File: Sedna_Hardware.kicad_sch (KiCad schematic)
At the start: 51 parts, among them J1 PJ-102A, J10 5-103634-2, J11 2-644488-2, J2 61201021721, J3 PPTC141LFBN-RC, J4 0878340619, J5 2-644803-3, J6 2-644488-3, J7 1935161, J8 1935161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

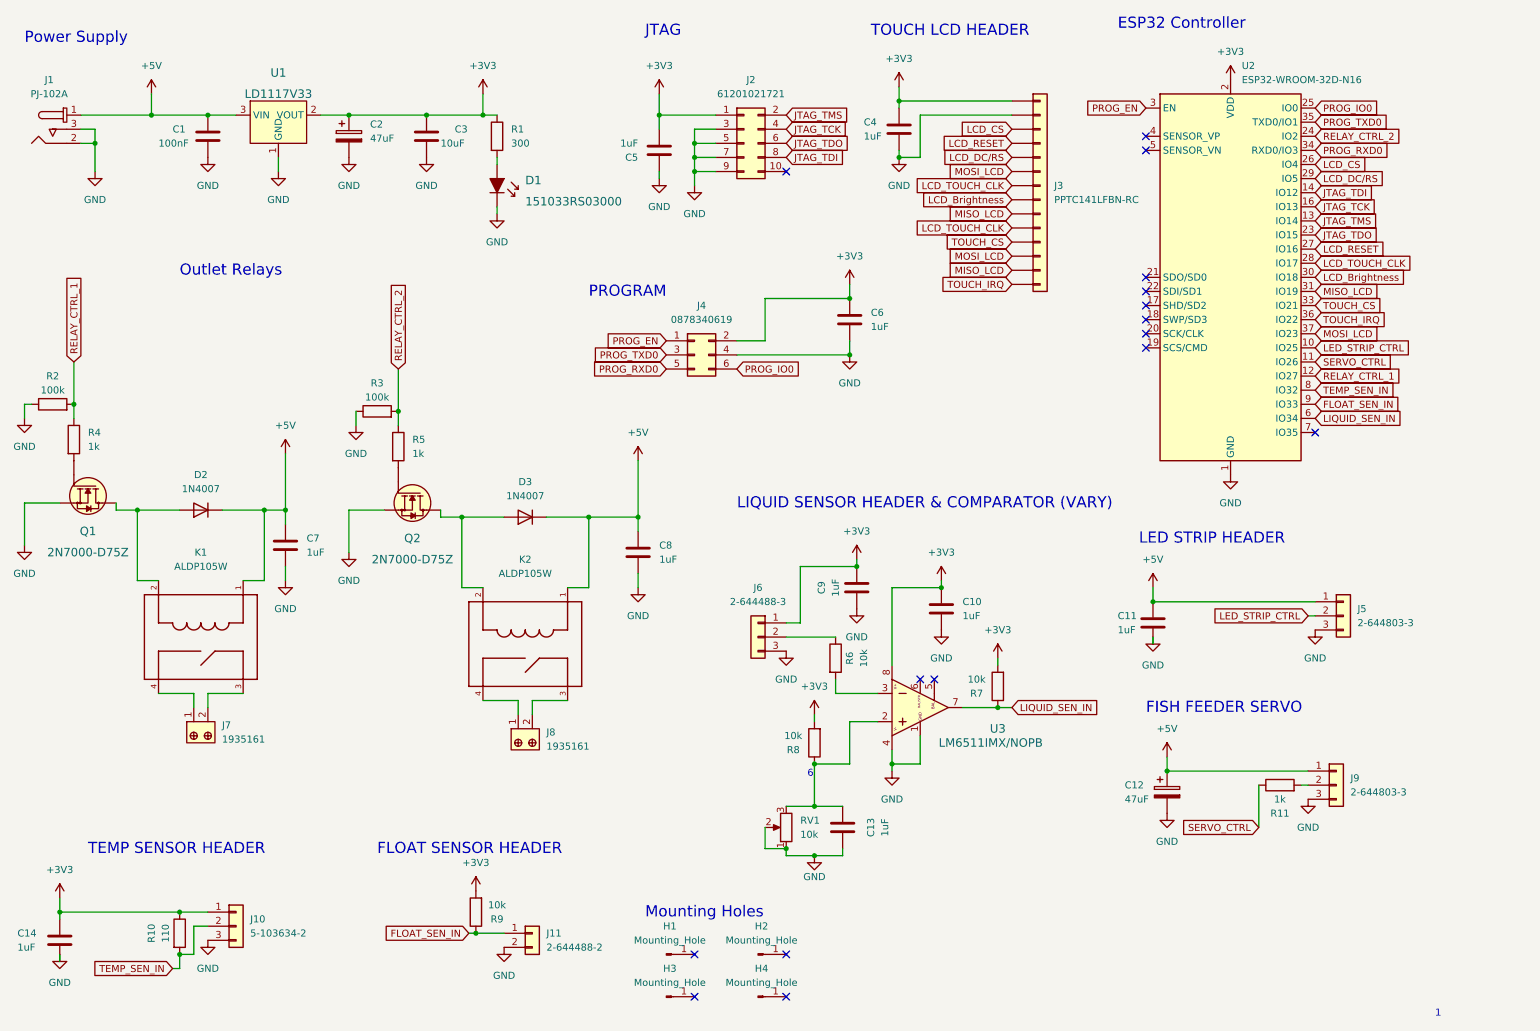
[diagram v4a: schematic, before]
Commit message: associated resistor and capacitor to DigiKey Procduct. Modified 1uf cap's footpring
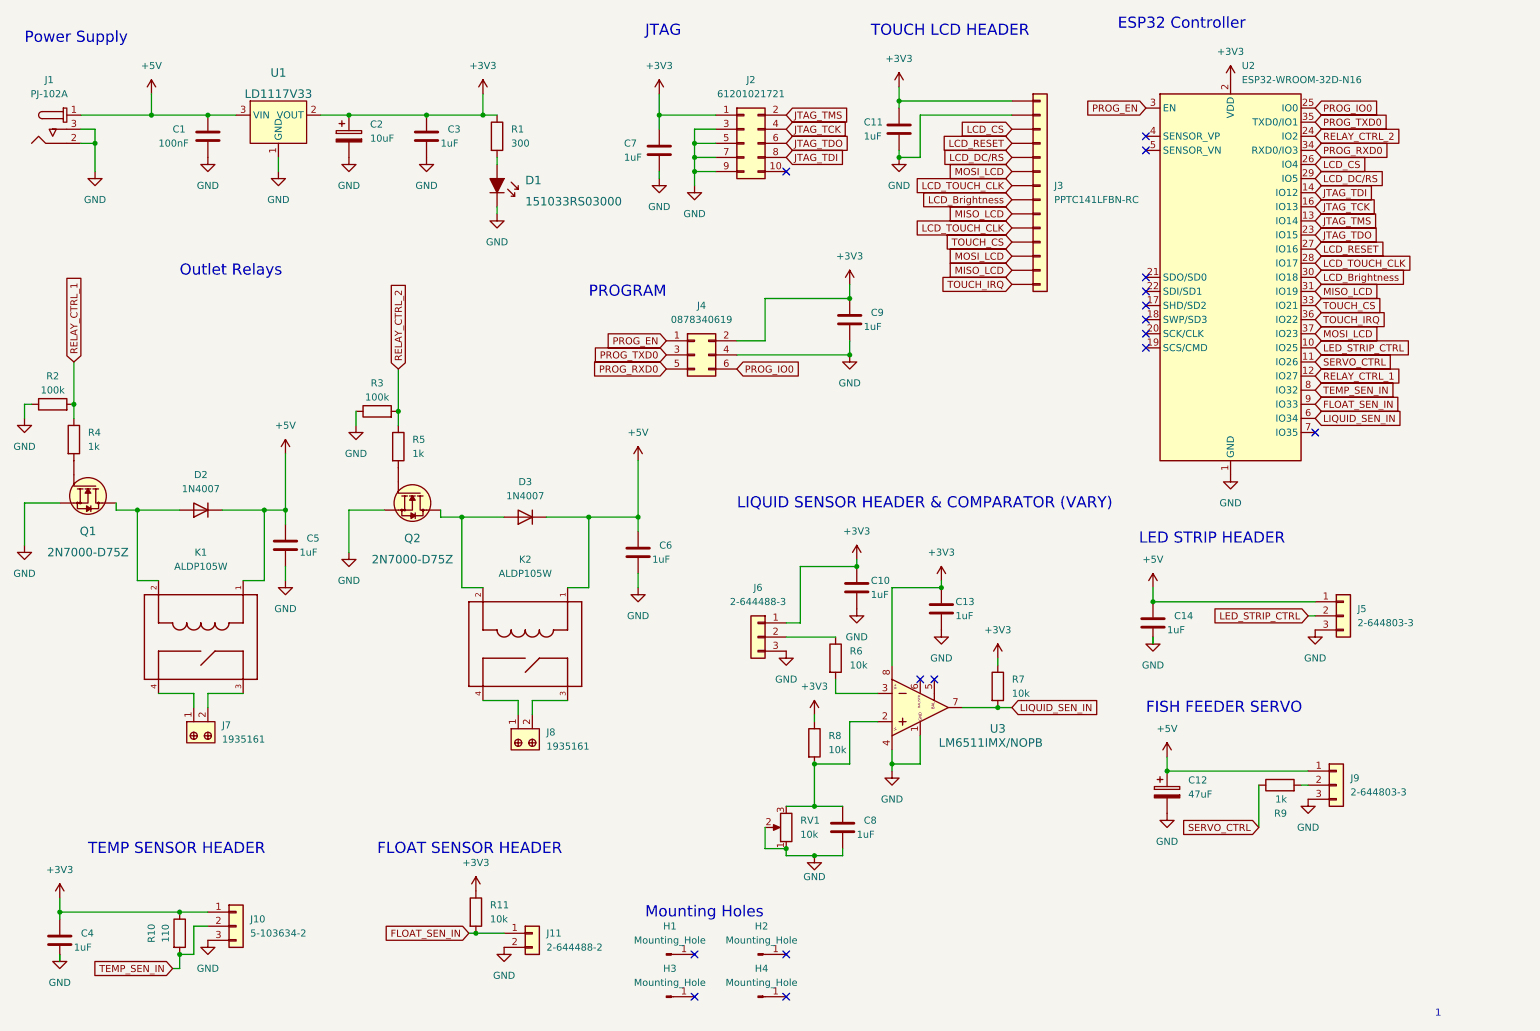
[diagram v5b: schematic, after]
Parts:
- C1: footprint Capacitor_THT:C_Disc_D9.0mm_W5.0mm_P5.00mm -> Capacitor_THT:C_Radial_D6.3mm_H5.0mm_P2.50mm; Category (none) -> Ceramic Capacitors; DK_Datasheet_LInk (none) -> https://www.vishay.com/docs/45171/kseries.pdf; DK_Detail_Page (none) -> https://www.digikey.ca/en/products/detail/vishay-beyschlag-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; Digi-key_PN (none) -> BC3324-ND; MPN (none) -> K104K15X7RF53L2; Manufacturer (none) -> Vishay Beyschlag/Draloric/BC Components; Status (none) -> active
- C10, C11, C13, C14, C4, C5, C6, C7, C8, C9: footprint Capacitor_THT:C_Disc_D9.0mm_W5.0mm_P5.00mm -> Capacitor_THT:C_Axial_L3.8mm_D2.6mm_P7.50mm_Horizontal; Category (none) -> Ceramic Capacitors; DK_Datasheet_Link (none) -> https://content.kemet.com/datasheets/KEM_C1041_AXIMAX_X7R.p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; DK_Detail_Page (none) -> https://www.digikey.ca/en/products/detail/kemet/C410C105K3R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; Digi-Key_PN (none) -> 399-C410C105K3R5TA-ND; MPN (none) -> C410C105K3R5TA; Manufacturer (none) -> KEMET; Status (none) -> active
- C12: Category (none) -> Aluminum Electrolytic Capacitors; DK_Datasheet_Link (none) -> https://media.digikey.com/pdf/Data%20Sheets/Panasonic%20Ele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; DK_Detail_Page (none) -> https://www.digikey.ca/en/products/detail/panasonic-electro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; Digi-Key_PN (none) -> P10417TB-ND; MPN (none) -> ECA-1VM470I; Manufacturer (none) -> Panasonic Electronic Components; Status (none) -> active
- C2: value 47uF -> 10uF; Category (none) -> Aluminum Electrolytic Capacitors; DK_Datasheet_Link (none) -> https://media.digikey.com/pdf/Data%20Sheets/Panasonic%20Ele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; DK_Detail_Page (none) -> https://www.digikey.ca/en/products/detail/kyocera-avx/TAP10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; Digi-Key_PN (none) -> 478-1839-ND; MPN (none) -> TAP106K016SCS; Manufacturer (none) -> KYOCERA AVX; Status (none) -> active
- C3: value 10uF -> 1uF; footprint Capacitor_THT:C_Disc_D9.0mm_W5.0mm_P5.00mm -> Capacitor_THT:C_Axial_L3.8mm_D2.6mm_P7.50mm_Horizontal; Category (none) -> Ceramic Capacitors; DK_Datasheet_Link (none) -> https://content.kemet.com/datasheets/KEM_C1041_AXIMAX_X7R.p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; DK_Detail_Page (none) -> https://www.digikey.ca/en/products/detail/kemet/C410C105K3R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; Digi-Key_PN (none) -> 399-C410C105K3R5TA-ND; MPN (none) -> C410C105K3R5TA; Manufacturer (none) -> KEMET; Status (none) -> active
- J2: Category (none) -> Rectangular Connectors - Headers, Male Pins; DK_Datasheet_Link (none) -> https://www.we-online.com/catalog/datasheet/61201021721.pdf; DK_Detail_Page (none) -> https://www.digikey.ca/en/products/detail/w%C3%BCrth-elektr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; Digi-Ket_PN (none) -> 732-2098-ND; MPN (none) -> 61201021721; Manufacturer (none) -> Würth Elektronik; Status (none) -> active
- R1: Category (none) -> Through Hole Resistors; DK_Datasheet_Link (none) -> https://www.vishay.com/docs/28766/mbxsma.pdf; DK_Detail_Page (none) -> https://www.digikey.ca/en/products/detail/vishay-beyschlag-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; Digi-Key_PN (none) -> BC3491TR-ND; MPN (none) -> MBA02040C3000FRP00; Manufacturer (none) -> Vishay Beyschlag/Draloric/BC Components; Status (none) -> active
- R10: Category (none) -> Through Hole Resistors; DK_Datasheet_Link (none) -> https://www.vishay.com/docs/28766/mbxsma.pdf; DK_Detail_Page (none) -> https://www.digikey.ca/en/products/detail/vishay-beyschlag-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; Digi-Key_PN (none) -> 56-MBA02040C1100FC100CT-ND; MPN (none) -> MBA02040C1100FC100; Manufacturer (none) -> Vishay Beyschlag/Draloric/BC Components; Status (none) -> active
- R11: value 1k -> 10k; Category (none) -> Through Hole Resistors; DK_Datasheet_Link (none) -> https://www.vishay.com/docs/28766/mbxsma.pdf; DK_Detail_Page (none) -> https://www.digikey.ca/en/products/detail/vishay-beyschlag-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; Digi-Key_PN (none) -> BC10.0KXTR-ND; MPN (none) -> MBA02040C1002FRP00; Manufacturer (none) -> Vishay Beyschlag/Draloric/BC Components; Status (none) -> active
- R2, R3: Category (none) -> Through Hole Resistors; DK_Datasheet_Link (none) -> https://www.vishay.com/docs/28766/mbxsma.pdf; DK_Detail_PAge (none) -> https://www.digikey.ca/en/products/detail/vishay-beyschlag-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; Digi-Key_PN (none) -> BC3240CT-ND; MPN (none) -> MBA02040C1003FCT00; Manufacturer (none) -> Vishay Beyschlag/Draloric/BC Components; Status (none) -> active
- R4, R5: Category (none) -> Through Hole Resistors; DK_Datasheet_Link (none) -> https://www.vishay.com/docs/28766/mbxsma.pdf; DK_Detail_Page (none) -> https://www.digikey.ca/en/products/detail/vishay-beyschlag-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; Digi-Key_PN (none) -> BC3238CT-ND; MPN (none) -> MBA02040C1001FCT00; Manufacturer (none) -> Vishay Beyschlag/Draloric/BC Components; Status (none) -> active
- R6, R7, R8: Category (none) -> Through Hole Resistors; DK_Datasheet_Link (none) -> https://www.vishay.com/docs/28766/mbxsma.pdf; DK_Detail_Page (none) -> https://www.digikey.ca/en/products/detail/vishay-beyschlag-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; Digi-Key_PN (none) -> BC10.0KXTR-ND; MPN (none) -> MBA02040C1002FRP00; Manufacturer (none) -> Vishay Beyschlag/Draloric/BC Components; Status (none) -> active
- R9: value 10k -> 1k; Category (none) -> Through Hole Resistors; DK_Datasheet_Link (none) -> https://www.vishay.com/docs/28766/mbxsma.pdf; DK_Detail_Page (none) -> https://www.digikey.ca/en/products/detail/vishay-beyschlag-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; Digi-Key_PN (none) -> BC3238CT-ND; MPN (none) -> MBA02040C1001FCT00; Manufacturer (none) -> Vishay Beyschlag/Draloric/BC Components; Status (none) -> active
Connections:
- net +3V3: now also C11.1, C13.1, C7.1, C9.1, R11.1, R7.1, R8.1; no longer C14.1, C5.2, C6.1, C9.2, R7.2, R8.2, R9.2
- net +5V: now also C14.1, C5.1, C6.1; no longer C11.1, C7.1, C8.1
- net FLOAT_SEN_IN: now also R11.2; no longer R9.1
- net GND: now also C13.2, C5.2, C9.2; no longer C13.1, C5.1, C9.1
- net LIQUID_SEN_IN: now also R7.2; no longer R7.1
- net SERVO_CTRL: now also R9.1; no longer R11.1
- net at J9.2 (Pin_2): now also R9.2; no longer R11.2
- net at RV1.3, U3.2: now also C8.1, R8.2; no longer C13.2, R8.1
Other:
- note removed: "6"

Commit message: Modified potentimeter footprint
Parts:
- RV1: footprint Potentiometer_THT:Potentiometer_Bourns_3296W_Vertical -> 3306K-1-103:TRIM_3306K-1-103; Category (none) -> Trimmer Potentiometers; DK_Datasheet_Link (none) -> https://www.bourns.com/docs/Product-Datasheets/3306.pdf; DK_Detail_Page (none) -> https://www.digikey.ca/en/products/detail/bourns-inc/3306K-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; Digi-Key_PN (none) -> 3306K-103-ND; MPN (none) -> 3306K-1-103; Manufacturer (none) -> Bourns Inc.; Status (none) -> active
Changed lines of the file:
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@@
       (effects (font (size 1.27 1.27)) (justify right))
     )
-    (property "Footprint" "Potentiometer_THT:Potentiometer_Bourns_3296W_Vertical" (id 2) (at 152.4 160.02 0)
-      (effects (font (size 1.27 1.27)) hide)
-    )
-    (property "Datasheet" "~" (id 3) (at 152.4 160.02 0)
+    (property "Footprint" "3306K-1-103:TRIM_3306K-1-103" (id 2) (at 152.4 160.02 0)
+      (effects (font (size 1.27 1.27)) hide)
+    )
+    (property "Datasheet" "https://www.bourns.com/docs/Product-Datasheets/3306.pdf" (id 3) (at 152.4 160.02 0)
+      (effects (font (size 1.27 1.27)) hide)
+    )
+    (property "Digi-Key_PN" "3306K-103-ND" (id 4) (at 152.4 160.02 0)
+      (effects (font (size 1.27 1.27)) hide)
+    )
+    (property "MPN" "3306K-1-103" (id 5) (at 152.4 160.02 0)
+      (effects (font (size 1.27 1.27)) hide)
+    )
+    (property "Category" "Trimmer Potentiometers" (id 6) (at 152.4 160.02 0)
+      (effects (font (size 1.27 1.27)) hide)
+    )
+    (property "DK_Datasheet_Link" "https://www.bourns.com/docs/Product-Datasheets/3306.pdf" (id 7) (at 152.4 160.02 0)
+      (effects (font (size 1.27 1.27)) hide)
+    )
+    (property "DK_Detail_Page" "https://www.digikey.ca/en/products/detail/bourns-inc/3306K-1-103/84851" (id 8) (at 152.4 160.02 0)
+      (effects (font (size 1.27 1.27)) hide)
+    )
+    (property "Description" "TRIMMER 10K OHM 0.5W PC PIN TOP" (id 9) (at 152.4 160.02 0)
+      (effects (font (size 1.27 1.27)) hide)
+    )
+    (property "Manufacturer" "Bourns Inc." (id 10) (at 152.4 160.02 0)
+      (effects (font (size 1.27 1.27)) hide)
+    )
+    (property "Status" "active" (id 11) (at 152.4 160.02 0)
       (effects (font (size 1.27 1.27)) hide)
     )
@@
     )
     (path "/2fc025c7-eccb-4094-b36c-24387384df3a"
-      (reference "RV1") (unit 1) (value "10k") (footprint "Potentiometer_THT:Potentiometer_Bourns_3296W_Vertical")
+      (reference "RV1") (unit 1) (value "10k") (footprint "3306K-1-103:TRIM_3306K-1-103")
     )
     (path "/36e2d2d1-f78a-48a8-9b61-0b468dc7b54c"

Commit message: cleaned up symbol properties of several components
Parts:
- C1: Digi-Key_PN (none) -> BC3324-ND; Digi-key_PN BC3324-ND -> (none)
- D2, D3: DK_Datasheet_Link (none) -> https://www.vishay.com/docs/88503/1n4001.pdf; DK_Datasheet_link https://www.vishay.com/docs/88503/1n4001.pdf -> (none)
- J11: Mating_CONN (none) -> 3-644043-2; Mating_Conn 3-644043-2 -> (none)
- J2: Digi-Ket_PN 732-2098-ND -> (none); Digi-Key_PN (none) -> 732-2098-ND
- K1: Manifacturer Panasonic Electric Works -> (none); Manufacturer (none) -> Panasonic Electric Works
- K2: MF Panasonic -> (none); Manifacturer Panasonic Electric Works -> (none); Manufacturer (none) -> Panasonic Electric Works; PARTREV N/A -> (none); STANDART Manufacturer Recommendations -> (none)
- R2, R3: DK_Detail_PAge https://www.digikey.ca/en/products/detail/vishay-beyschlag-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 -> (none); DK_Detail_Page (none) -> https://www.digikey.ca/en/products/detail/vishay-beyschlag-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
- U2: Category (none) -> RF Transceiver Modules and Modems; DK_Datasheet_Link (none) -> https://www.espressif.com/sites/default/files/documentation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; DK_Detail_Page (none) -> https://www.digikey.ca/en/products/detail/espressif-systems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; Digi-Key_PN (none) -> 1965-ESP32-WROOM-32D-N16TR-ND; MPN (none) -> ESP32-WROOM-32D-N16; Manufacturer (none) -> Espressif Systems; Status (none) -> active
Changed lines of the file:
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@@
       (effects (font (size 1.27 1.27)) hide)
     )
-    (property "Mating_Conn" "3-644043-2" (id 13) (at 106.68 179.07 0)
+    (property "Mating_CONN" "3-644043-2" (id 13) (at 106.68 179.07 0)
       (effects (font (size 1.27 1.27)) hide)
     )
@@
       (effects (font (size 1.27 1.27)) hide)
     )
-    (property "Manifacturer" "Panasonic Electric Works" (id 11) (at 105.41 127 90)
+    (property "Manufacturer" "Panasonic Electric Works" (id 11) (at 105.41 127 90)
       (effects (font (size 1.27 1.27)) hide)
     )
     (property "Status" "Active" (id 12) (at 105.41 127 90)
       (effects (font (size 1.27 1.27)) hide)
-    )
-    (property "MF" "Panasonic" (id 13) (at 105.41 127 0)
-      (effects (font (size 1.27 1.27)) (justify left bottom) hide)
-    )
-    (property "PARTREV" "N/A" (id 14) (at 105.41 127 0)
-      (effects (font (size 1.27 1.27)) (justify left bottom) hide)
-    )
-    (property "STANDART" "Manufacturer Recommendations" (id 15) (at 105.41 127 0)
-      (effects (font (size 1.27 1.27)) (justify left bottom) hide)
     )
     (pin "1")
@@
     )
     (property "Datasheet" "https://www.espressif.com/sites/default/files/documentation/esp32-wroom-32d_esp32-wroom-32u_datasheet_en.pdf" (id 3) (at 224.79 59.69 0)
+      (effects (font (size 1.27 1.27)) hide)
+    )
+    (property "Digi-Key_PN" "1965-ESP32-WROOM-32D-N16TR-ND" (id 4) (at 232.41 60.96 0)
+      (effects (font (size 1.27 1.27)) hide)
+    )
+    (property "MPN" "ESP32-WROOM-32D-N16" (id 5) (at 232.41 60.96 0)
+      (effects (font (size 1.27 1.27)) hide)
+    )
+    (property "Category" "RF Transceiver Modules and Modems" (id 6) (at 232.41 60.96 0)
+      (effects (font (size 1.27 1.27)) hide)
+    )
+    (property "DK_Datasheet_Link" "https://www.espressif.com/sites/default/files/documentation/esp32-wroom-32d_esp32-wroom-32u_datasheet_en.pdf" (id 7) (at 232.41 60.96 0)
+      (effects (font (size 1.27 1.27)) hide)
+    )
+    (property "DK_Detail_Page" "https://www.digikey.ca/en/products/detail/espressif-systems/ESP32-WROOM-32D-N16/9381718?s=N4IgTCBcDaIKYGcAOBmMBaA7gJwPa4Ft00ARdAOQEYA2EAXQF8g" (id 8) (at 232.41 60.96 0)
+      (effects (font (size 1.27 1.27)) hide)
+    )
+    (property "Description" "RX TXRX MOD WIFI TRACE ANT SMD" (id 9) (at 232.41 60.96 0)
+      (effects (font (size 1.27 1.27)) hide)
+    )
+    (property "Manufacturer" "Espressif Systems" (id 10) (at 232.41 60.96 0)
+      (effects (font (size 1.27 1.27)) hide)
+    )
+    (property "Status" "active" (id 11) (at 232.41 60.96 0)
       (effects (font (size 1.27 1.27)) hide)
     )
@@
       (effects (font (size 1.27 1.27)) hide)
     )
-    (property "DK_Detail_PAge" "https://www.digikey.ca/en/products/detail/vishay-beyschlag-draloric-bc-components/MBA02040C1003FCT00/6138743" (id 8) (at 78.74 85.09 90)
+    (property "DK_Detail_Page" "https://www.digikey.ca/en/products/detail/vishay-beyschlag-draloric-bc-components/MBA02040C1003FCT00/6138743" (id 8) (at 78.74 85.09 90)
       (effects (font (size 1.27 1.27)) hide)
     )
@@
       (effects (font (size 1.27 1.27)) hide)
     )
-    (property "Manifacturer" "Panasonic Electric Works" (id 11) (at 46.99 125.73 90)
+    (property "Manufacturer" "Panasonic Electric Works" (id 11) (at 46.99 125.73 90)
       (effects (font (size 1.27 1.27)) hide)
     )
@@
       (effects (font (size 1.27 1.27)) hide)
     )
-    (property "Digi-key_PN" "BC3324-ND" (id 4) (at 48.26 35.56 0)
+    (property "Digi-Key_PN" "BC3324-ND" (id 4) (at 48.26 35.56 0)
       (effects (font (size 1.27 1.27)) hide)
     )
@@
       (effects (font (size 1.27 1.27)) hide)
     )
-    (property "DK_Detail_PAge" "https://www.digikey.ca/en/products/detail/vishay-beyschlag-draloric-bc-components/MBA02040C1003FCT00/6138743" (id 8) (at 20.32 83.82 90)
+    (property "DK_Detail_Page" "https://www.digikey.ca/en/products/detail/vishay-beyschlag-draloric-bc-components/MBA02040C1003FCT00/6138743" (id 8) (at 20.32 83.82 90)
       (effects (font (size 1.27 1.27)) hide)
     )
@@
       (effects (font (size 1.27 1.27)) hide)
     )
-    (property "DK_Datasheet_link" "https://www.vishay.com/docs/88503/1n4001.pdf" (id 8) (at 105.41 104.14 0)
+    (property "DK_Datasheet_Link" "https://www.vishay.com/docs/88503/1n4001.pdf" (id 8) (at 105.41 104.14 0)
       (effects (font (size 1.27 1.27)) hide)
     )
@@
       (effects (font (size 1.27 1.27)) hide)
     )
-    (property "DK_Datasheet_link" "https://www.vishay.com/docs/88503/1n4001.pdf" (id 8) (at 46.99 102.87 0)
+    (property "DK_Datasheet_Link" "https://www.vishay.com/docs/88503/1n4001.pdf" (id 8) (at 46.99 102.87 0)
       (effects (font (size 1.27 1.27)) hide)
     )
@@
       (effects (font (size 1.27 1.27)) hide)
     )
-    (property "Digi-Ket_PN" "732-2098-ND" (id 4) (at 144.78 36.83 0)
-      (effects (font (size 1.27 1.27)) hide)
-    )
+    (property "Digi-Key_PN" "732-2098-ND" (id 4) (at 144.78 36.83 0)
+      (effects (font (size 1.27 1.27)) hide)
+    )

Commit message: fixed symbol properties again
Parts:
- C1: DK_Datasheet_LInk https://www.vishay.com/docs/45171/kseries.pdf -> (none); DK_Datasheet_Link (none) -> https://www.vishay.com/docs/45171/kseries.pdf
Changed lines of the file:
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@@
       (effects (font (size 1.27 1.27)) hide)
     )
-    (property "DK_Datasheet_LInk" "https://www.vishay.com/docs/45171/kseries.pdf" (id 7) (at 48.26 35.56 0)
+    (property "DK_Datasheet_Link" "https://www.vishay.com/docs/45171/kseries.pdf" (id 7) (at 48.26 35.56 0)
       (effects (font (size 1.27 1.27)) hide)
     )
